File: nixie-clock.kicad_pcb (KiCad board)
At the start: 2 copper layers, 148.3 x 67.6 mm, 53 parts, among them J1 Conn_01x05_Male, J2 Conn_01x02_Male, U1 K155ID1, U10 LD1117S33TR_SOT223, U11 TLP627-2, U2 74HC595, U3 TLP627-2, U4 K155ID1, U5 K155ID1, U6 74HC595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

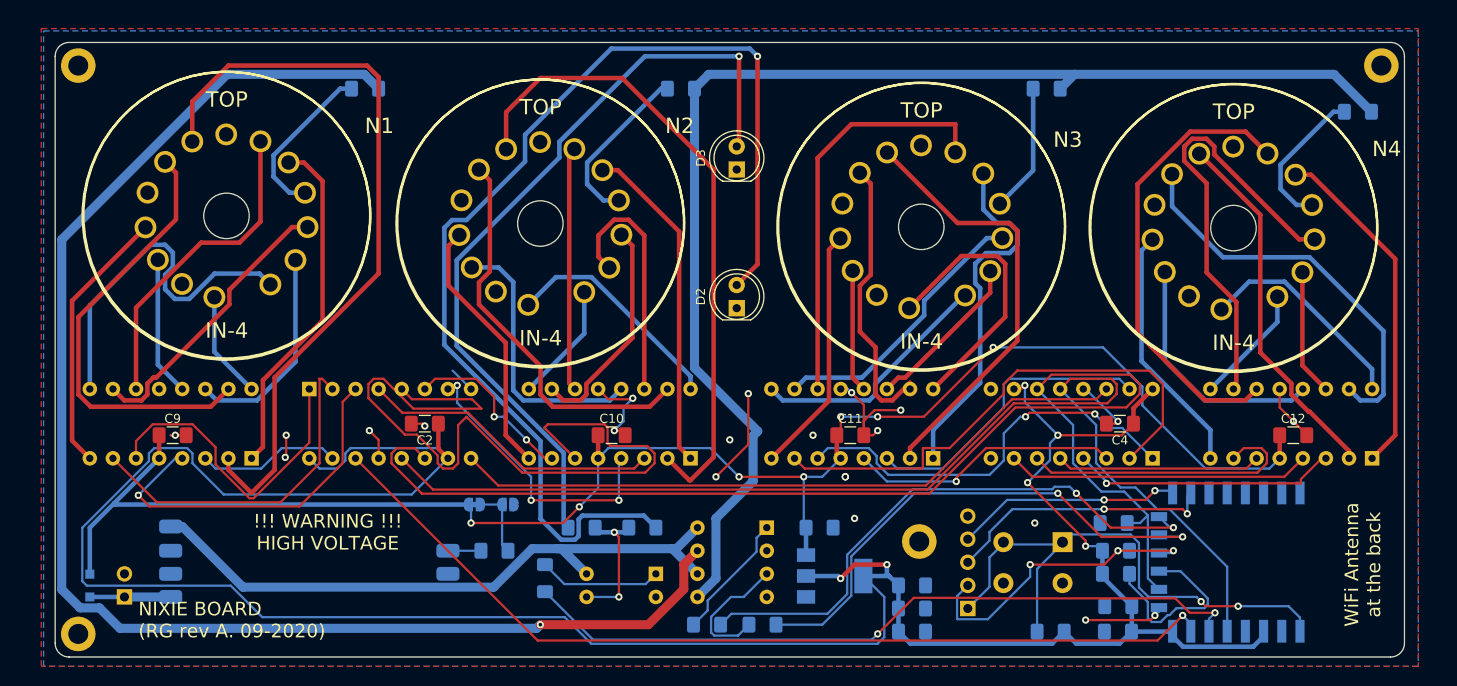
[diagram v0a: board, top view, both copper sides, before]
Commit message: Fix alignment on main board and add front and back board
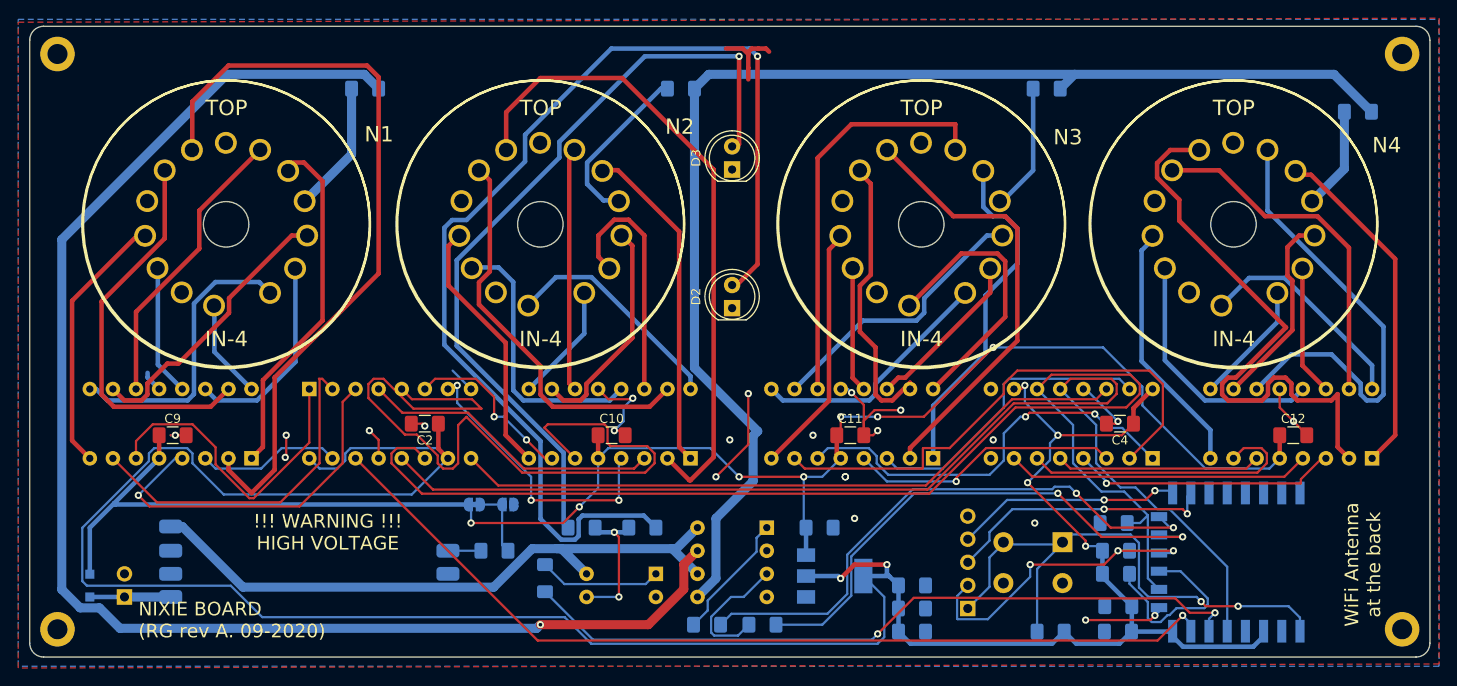
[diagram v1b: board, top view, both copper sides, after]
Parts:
- moved REF** 54.0 mm to (176.0, 84.8)
- moved REF** 2.62 mm to (176.0, 21.6)
- moved REF** 2.62 mm to (28.2, 21.6)
- moved REF** 2.34 mm to (28.2, 84.8)
- moved N1 0.93 mm to (46.8, 40.2)
- moved D2 0.51 mm to (102.4, 49.5)
- moved D3 0.51 mm to (102.4, 34.3)
- moved N4 0.41 mm to (157.5, 40.2)
- moved N3 0.28 mm to (123.2, 40.2)
- moved N2 0.09 mm to (81.3, 40.2)
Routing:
- net Net-(N4-Pad8): track 48.9 -> 22.0 mm
- net Net-(N4-Pad0): track 40.4 -> 64.3 mm
- net GND: track 69.7 -> 80.3 mm, vias 22 -> 23
- net Net-(N1-Pad4): track 39.5 -> 32.1 mm
- net Net-(N1-Pad2): track 48.4 -> 42.8 mm
- net Net-(N4-Pad2): track 44.0 -> 38.5 mm
- net Net-(N4-PadA3): track 16.3 -> 11.3 mm
- net Net-(N1-PadA3): track 18.2 -> 14.5 mm
- net Net-(N1-Pad7): track 35.4 -> 31.9 mm
- net Net-(N3-Pad9): track 39.5 -> 37.8 mm
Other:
- board size 148.3 x 67.6 mm -> 153.9 x 69.3 mm
- board text added: "0"
- board text added: "GND"
- board text added: "RST"
- board text added: "RX"
- board text added: "TX"
